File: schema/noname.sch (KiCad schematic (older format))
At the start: 7 parts

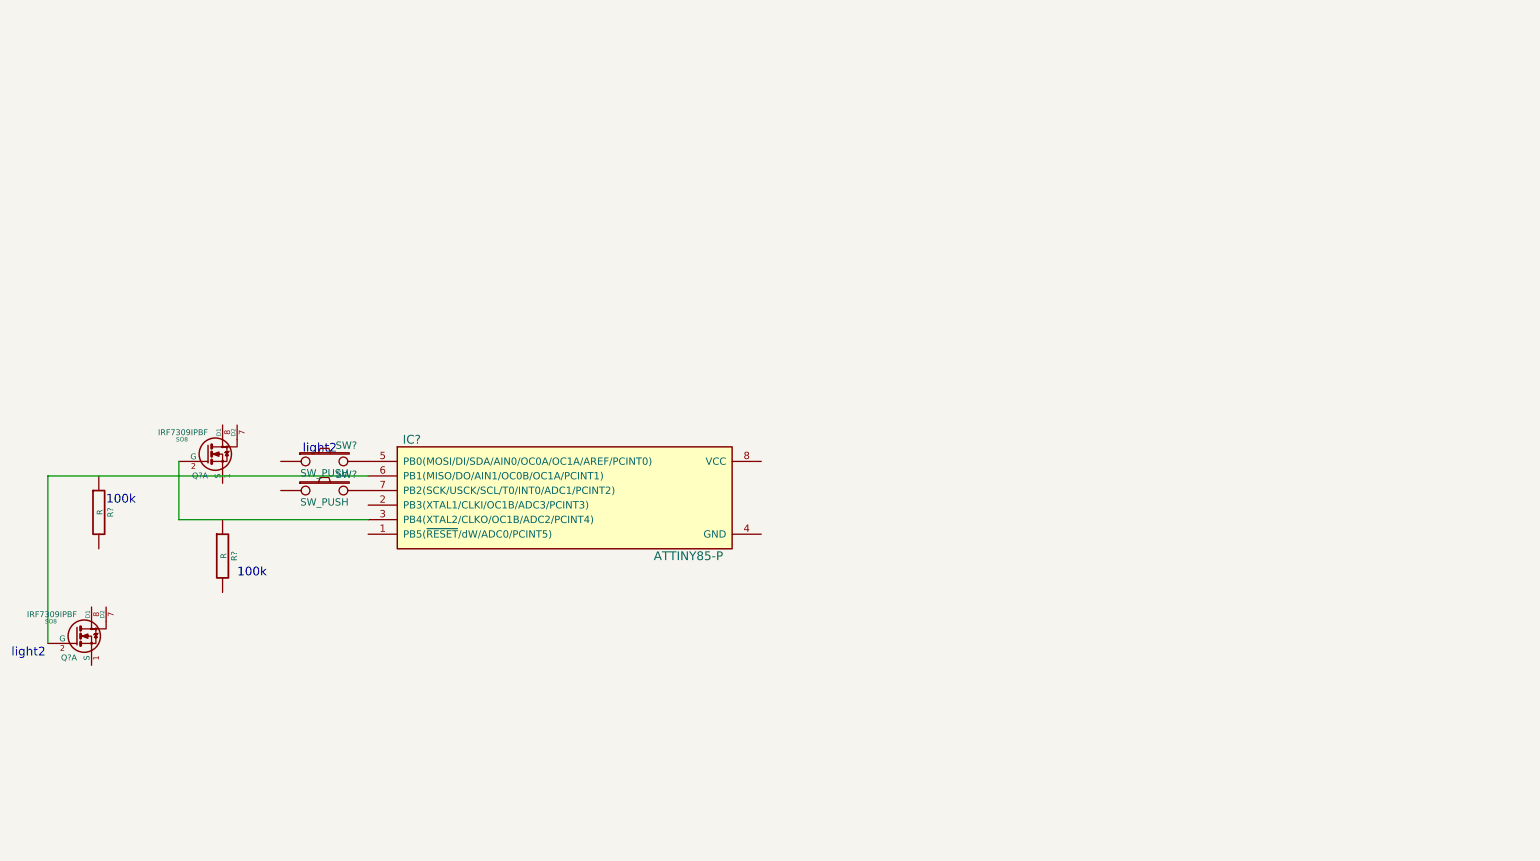
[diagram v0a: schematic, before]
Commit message: Use other pins
The Trinket boot makes the led flicker at startup (even without usb
connection). Use other pins that are not used by the boot software.
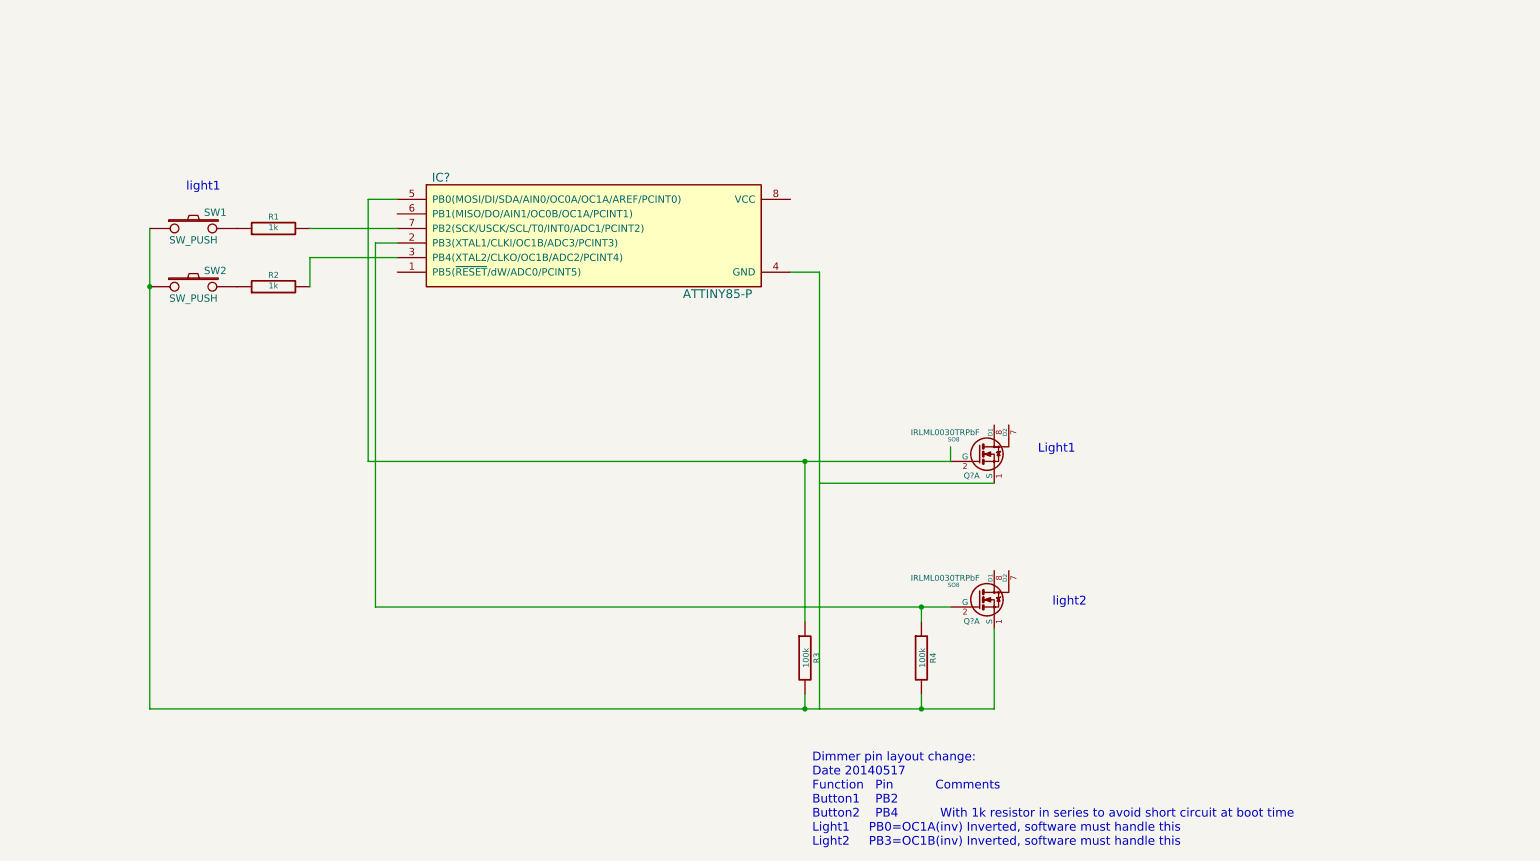
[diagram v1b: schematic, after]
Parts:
- added R1, R2: 1k, ~, symbol R
- Q? (x2): value IRF7309IPBF -> IRLML0030TRPbF
- R3, R4: renamed from R?; value R -> 100k
- gave numbers to parts that had none: 2
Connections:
- wire segments 4 -> 20
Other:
- note added: "Dimmer pin layout change:\nDate 20140517\nFunction Pin Comments\nButton1 PB2\nButton2 PB4 With 1k resistor in series to avoid short circuit at boot time\nLight1 PB0=OC1A(inv) Inverted, software must handle this\nLight2 PB3=OC1B(inv) Inverted, software must handle this"
- note added: "Light1"
- note added: "light1\n"
- note removed: "100k"
- note removed: "light2"
- moved on the sheet: IC?, Q?A, R3, R4, SW1, SW2
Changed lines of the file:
@@
 LIBS:contrib
 LIBS:valves
+LIBS:noname-cache
 EELAYER 27 0
 EELAYER END
@@
 Sheet 1 1
 Title "noname.sch"
-Date "15 may 2014"
+Date "17 may 2014"
 Rev ""
 Comp ""
@@
 L ATTINY85-P IC?
 U 1 1 53752E2B
-P 5050 3550
-F 0 "IC?" H 4000 3950 60  0000 C CNN
-F 1 "ATTINY85-P" H 5900 3150 60  0000 C CNN
-F 2 "DIP8" H 4000 3150 60  0001 C CNN
-F 3 "" H 5050 3550 60  0000 C CNN
-	1    5050 3550
+P 5250 1750
+F 0 "IC?" H 4200 2150 60  0000 C CNN
+F 1 "ATTINY85-P" H 6100 1350 60  0000 C CNN
+F 2 "DIP8" H 4200 1350 60  0001 C CNN
+F 3 "" H 5250 1750 60  0000 C CNN
+	1    5250 1750
 	1    0    0    -1
 $EndComp
@@
 L IRF7309IPBF Q?
 U 1 1 53752E93
-P 2600 3250
-F 0 "Q?" H 2600 3102 40  0000 R CNN
-F 1 "IRF7309IPBF" H 2600 3399 40  0000 R CNN
-F 2 "SO8" H 2421 3351 29  0000 C CNN
-F 3 "~" H 2600 3250 60  0000 C CNN
-	1    2600 3250
+P 7900 3250
+F 0 "Q?" H 7900 3102 40  0000 R CNN
+F 1 "IRLML0030TRPbF" H 7900 3399 40  0000 R CNN
+F 2 "SO8" H 7721 3351 29  0000 C CNN
+F 3 "~" H 7900 3250 60  0000 C CNN
+	1    7900 3250
 	1    0    0    -1
 $EndComp
-Wire Wire Line
-	3700 3700 2400 3700
-Wire Wire Line
-	2400 3700 2400 3300
 $Comp
 L IRF7309IPBF Q?
 U 1 1 53752F5C
-P 1700 4500
-F 0 "Q?" H 1700 4352 40  0000 R CNN
-F 1 "IRF7309IPBF" H 1700 4649 40  0000 R CNN
-F 2 "SO8" H 1521 4601 29  0000 C CNN
-F 3 "~" H 1700 4500 60  0000 C CNN
-	1    1700 4500
+P 7900 4250
+F 0 "Q?" H 7900 4102 40  0000 R CNN
+F 1 "IRLML0030TRPbF" H 7900 4399 40  0000 R CNN
+F 2 "SO8" H 7721 4351 29  0000 C CNN
+F 3 "~" H 7900 4250 60  0000 C CNN
+	1    7900 4250
 	1    0    0    -1
 $EndComp
 $Comp
-L R R?
+L R R4
 U 1 1 53753193
-P 2700 3950
-F 0 "R?" V 2780 3950 40  0000 C CNN
-F 1 "R" V 2707 3951 40  0000 C CNN
-F 2 "~" V 2630 3950 30  0000 C CNN
-F 3 "~" H 2700 3950 30  0000 C CNN
-	1    2700 3950
+P 7500 4650
+F 0 "R4" V 7580 4650 40  0000 C CNN
+F 1 "100k" V 7507 4651 40  0000 C CNN
+F 2 "~" V 7430 4650 30  0000 C CNN
+F 3 "~" H 7500 4650 30  0000 C CNN
+	1    7500 4650
 	1    0    0    -1
 $EndComp
 $Comp
-L SW_PUSH SW?
+L SW_PUSH SW1
 U 1 1 5375321D
-P 3400 3500
-F 0 "SW?" H 3550 3610 50  0000 C CNN
-F 1 "SW_PUSH" H 3400 3420 50  0000 C CNN
-F 2 "~" H 3400 3500 60  0000 C CNN
-F 3 "~" H 3400 3500 60  0000 C CNN
-	1    3400 3500
+P 2500 1700
+F 0 "SW1" H 2650 1810 50  0000 C CNN
+F 1 "SW_PUSH" H 2500 1620 50  0000 C CNN
+F 2 "~" H 2500 1700 60  0000 C CNN
+F 3 "~" H 2500 1700 60  0000 C CNN
+	1    2500 1700
 	1    0    0    -1
 $EndComp
 $Comp
-L SW_PUSH SW?
+L SW_PUSH SW2
 U 1 1 53753232
-P 3400 3300
-F 0 "SW?" H 3550 3410 50  0000 C CNN
-F 1 "SW_PUSH" H 3400 3220 50  0000 C CNN
-F 2 "~" H 3400 3300 60  0000 C CNN
-F 3 "~" H 3400 3300 60  0000 C CNN
-	1    3400 3300
+P 2500 2100
+F 0 "SW2" H 2650 2210 50  0000 C CNN
+F 1 "SW_PUSH" H 2500 2020 50  0000 C CNN
+F 2 "~" H 2500 2100 60  0000 C CNN
+F 3 "~" H 2500 2100 60  0000 C CNN
+	1    2500 2100
 	1    0    0    -1
 $EndComp
-Text Notes 3250 3250 0    60   ~ 0
-light2\n
-Text Notes 1250 4650 0    60   ~ 0
-light2
-Wire Wire Line
-	3700 3400 1500 3400
-Wire Wire Line
-	1500 3400 1500 4550
-Text Notes 2800 4100 0    60   ~ 0
-100k
 $Comp
-L R R?
+L R R3
 U 1 1 53753325
-P 1850 3650
-F 0 "R?" V 1930 3650 40  0000 C CNN
-F 1 "R" V 1857 3651 40  0000 C CNN
-F 2 "~" V 1780 3650 30  0000 C CNN
-F 3 "~" H 1850 3650 30  0000 C CNN
-	1    1850 3650
+P 6700 4650
+F 0 "R3" V 6780 4650 40  0000 C CNN
+F 1 "100k" V 6707 4651 40  0000 C CNN
+F 2 "~" V 6630 4650 30  0000 C CNN
+F 3 "~" H 6700 4650 30  0000 C CNN
+	1    6700 4650
 	1    0    0    -1
 $EndComp
-Text Notes 1900 3600 0    60   ~ 0
-100k
+Text Notes 6750 5950 0    60   ~ 0
+Dimmer pin layout change:\nDate 20140517\nFunction   Pin           Comments\nButton1    PB2\nButton2    PB4           With 1k resistor in series to avoid short circuit at boot time\nLight1     PB0=OC1A(inv) Inverted, software must handle this\nLight2     PB3=OC1B(inv) Inverted, software must handle this
+Text Notes 8400 4300 0    60   ~ 0
+light2\n
+Text Notes 2450 1450 0    60   ~ 0
+light1\n
+$Comp
+L R R1
+U 1 1 53772E95
+P 3050 1700
+F 0 "R1" V 3130 1700 40  0000 C CNN
+F 1 "1k" V 3057 1701 40  0000 C CNN
+F 2 "~" V 2980 1700 30  0000 C CNN
+F 3 "~" H 3050 1700 30  0000 C CNN
+	1    3050 1700
+	0    -1   -1   0
+$EndComp
+$Comp
+L R R2
+U 1 1 53772EA2
+P 3050 2100
+F 0 "R2" V 3130 2100 40  0000 C CNN
+F 1 "1k" V 3057 2101 40  0000 C CNN
+F 2 "~" V 2980 2100 30  0000 C CNN
+F 3 "~" H 3050 2100 30  0000 C CNN
+	1    3050 2100
+	0    -1   -1   0
+$EndComp
+Wire Wire Line
+	3300 1700 3900 1700
+Wire Wire Line
+	3300 2100 3300 1900
+Wire Wire Line
+	3300 1900 3900 1900
+Wire Wire Line
+	7700 3200 7700 3300
+Wire Wire Line
+	3900 1500 3700 1500
+Wire Wire Line
+	3700 1500 3700 3300
+Wire Wire Line
+	3700 3300 7700 3300
+Wire Wire Line
+	3900 1800 3750 1800
+Wire Wire Line
+	3750 1800 3750 4300
+Wire Wire Line
+	3750 4300 7700 4300
+Wire Wire Line
+	6700 4400 6700 3300
+Connection ~ 6700 3300
+Wire Wire Line
+	7500 4400 7500 4300
+Connection ~ 7500 4300
+Wire Wire Line
+	8000 3450 6800 3450
+Wire Wire Line
+	6800 2000 6800 5000
+Wire Wire Line
+	6800 2000 6600 2000
+Wire Wire Line
+	6700 4900 6700 5000
+Wire Wire Line
+	2200 5000 8000 5000
+Wire Wire Line
+	7500 5000 7500 4900
+Wire Wire Line
+	8000 5000 8000 4450
+Connection ~ 7500 5000
+Wire Wire Line
+	2200 1700 2200 5000
+Connection ~ 6700 5000
+Connection ~ 2200 2100
+Text Notes 8300 3250 0    60   ~ 0
+Light1
 $EndSCHEMATC

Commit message: added fet footprint in schema
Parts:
- removed Q? (x2): IRLML0030TRPbF, SO8, symbol IRF7309IPBF
- added Q? (x2): IRLML0030TRPBF, SOT-23, symbol IRLML0030TRPBF
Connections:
- wire segments 20 -> 21
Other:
- note added: "1"
- note added: "2"
- note added: "3"
- note added: "SOT-23"
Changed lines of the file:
@@
-$EndComp
-$Comp
-L IRF7309IPBF Q?
-U 1 1 53752E93
-P 7900 3250
-F 0 "Q?" H 7900 3102 40  0000 R CNN
-F 1 "IRLML0030TRPbF" H 7900 3399 40  0000 R CNN
-F 2 "SO8" H 7721 3351 29  0000 C CNN
-F 3 "~" H 7900 3250 60  0000 C CNN
-	1    7900 3250
-	1    0    0    -1
-$EndComp
-$Comp
-L IRF7309IPBF Q?
-U 1 1 53752F5C
-P 7900 4250
-F 0 "Q?" H 7900 4102 40  0000 R CNN
-F 1 "IRLML0030TRPbF" H 7900 4399 40  0000 R CNN
-F 2 "SO8" H 7721 4351 29  0000 C CNN
-F 3 "~" H 7900 4250 60  0000 C CNN
-	1    7900 4250
-	1    0    0    -1
 $EndComp
 $Comp
@@
 Text Notes 8300 3250 0    60   ~ 0
 Light1
+$Comp
+L IRLML0030TRPBF Q?
+U 1 1 53774EA5
+P 7900 3150
+F 0 "Q?" H 7900 3002 40  0000 R CNN
+F 1 "IRLML0030TRPBF" H 7900 3299 40  0000 R CNN
+F 2 "SOT-23" H 7721 3251 29  0000 C CNN
+F 3 "~" H 7900 3150 60  0000 C CNN
+	1    7900 3150
+	1    0    0    -1
+$EndComp
+$Comp
+L IRLML0030TRPBF Q?
+U 1 1 53774EB4
+P 7900 4250
+F 0 "Q?" H 7900 4102 40  0000 R CNN
+F 1 "IRLML0030TRPBF" H 7900 4399 40  0000 R CNN
+F 2 "SOT-23" H 7721 4351 29  0000 C CNN
+F 3 "~" H 7900 4250 60  0000 C CNN
+	1    7900 4250
+	1    0    0    -1
+$EndComp
+Wire Wire Line
+	8000 3450 8000 3350
+Wire Notes Line
+	7100 2200 7400 2200
+Wire Notes Line
+	7400 2200 7400 2650
+Wire Notes Line
+	7400 2650 7100 2650
+Wire Notes Line
+	7100 2650 7100 2200
+Wire Notes Line
+	7100 2300 7050 2300
+Wire Notes Line
+	7050 2300 7050 2350
+Wire Notes Line
+	7050 2350 7100 2350
+Wire Notes Line
+	7100 2550 7050 2550
+Wire Notes Line
+	7050 2550 7050 2500
+Wire Notes Line
+	7050 2500 7100 2500
+Wire Notes Line
+	7400 2400 7450 2400
+Wire Notes Line
+	7450 2400 7450 2450
+Wire Notes Line
+	7450 2450 7400 2450
+Text Notes 6950 2300 0    60   ~ 0
+1
+Text Notes 6950 2550 0    60   ~ 0
+2
+Text Notes 7500 2400 0    60   ~ 0
+3
+Text Notes 7000 2100 0    60   ~ 0
+SOT-23
+Connection ~ 6800 5000
+Connection ~ 6700 4400
+Connection ~ 7500 4400
+Connection ~ 7500 4900
+Connection ~ 6700 4900
+Connection ~ 7700 4300
+Connection ~ 8000 4450
+Connection ~ 6800 3450
+Connection ~ 7700 3200
+Connection ~ 8000 3350
+Connection ~ 6600 2000
+Connection ~ 3900 1900
+Connection ~ 3900 1800
+Connection ~ 3900 1700
+Connection ~ 3900 1500
+Connection ~ 3300 1700
+Connection ~ 3300 2100
+Connection ~ 2800 2100
+Connection ~ 2800 1700
+Connection ~ 2200 1700
 $EndSCHEMATC

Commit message: Schema updated, software updated
This works (tested) for light 1.
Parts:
- added R5, R6: 22k, ~, symbol R
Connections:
- wire segments 21 -> 20
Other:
- moved on the sheet: R4
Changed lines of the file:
@@
 Sheet 1 1
 Title "noname.sch"
-Date "17 may 2014"
+Date "22 may 2014"
 Rev ""
 Comp ""
@@
 L R R4
 U 1 1 53753193
-P 7500 4650
-F 0 "R4" V 7580 4650 40  0000 C CNN
-F 1 "100k" V 7507 4651 40  0000 C CNN
-F 2 "~" V 7430 4650 30  0000 C CNN
-F 3 "~" H 7500 4650 30  0000 C CNN
-	1    7500 4650
+P 7000 4650
+F 0 "R4" V 7080 4650 40  0000 C CNN
+F 1 "100k" V 7007 4651 40  0000 C CNN
+F 2 "~" V 6930 4650 30  0000 C CNN
+F 3 "~" H 7000 4650 30  0000 C CNN
+	1    7000 4650
 	1    0    0    -1
 $EndComp
@@
 	3300 1900 3900 1900
 Wire Wire Line
-	7700 3200 7700 3300
-Wire Wire Line
 	3900 1500 3700 1500
 Wire Wire Line
-	3700 1500 3700 3300
-Wire Wire Line
-	3700 3300 7700 3300
-Wire Wire Line
 	3900 1800 3750 1800
 Wire Wire Line
 	3750 1800 3750 4300
 Wire Wire Line
-	3750 4300 7700 4300
-Wire Wire Line
-	6700 4400 6700 3300
-Connection ~ 6700 3300
-Wire Wire Line
-	7500 4400 7500 4300
-Connection ~ 7500 4300
-Wire Wire Line
 	8000 3450 6800 3450
 Wire Wire Line
@@
 	2200 5000 8000 5000
 Wire Wire Line
-	7500 5000 7500 4900
-Wire Wire Line
 	8000 5000 8000 4450
-Connection ~ 7500 5000
 Wire Wire Line
 	2200 1700 2200 5000
@@
 Connection ~ 6800 5000
 Connection ~ 6700 4400
-Connection ~ 7500 4400
-Connection ~ 7500 4900
 Connection ~ 6700 4900
 Connection ~ 7700 4300
@@
 Connection ~ 2800 1700
 Connection ~ 2200 1700
+$Comp
+L R R5
+U 1 1 537E6BFB
+P 7450 3200
+F 0 "R5" V 7530 3200 40  0000 C CNN
+F 1 "22k" V 7457 3201 40  0000 C CNN
+F 2 "~" V 7380 3200 30  0000 C CNN
+F 3 "~" H 7450 3200 30  0000 C CNN
+	1    7450 3200
+	0    -1   -1   0
+$EndComp
+$Comp
+L R R6
+U 1 1 537E6C0A
+P 7450 4300
+F 0 "R6" V 7530 4300 40  0000 C CNN
+F 1 "22k" V 7457 4301 40  0000 C CNN
+F 2 "~" V 7380 4300 30  0000 C CNN
+F 3 "~" H 7450 4300 30  0000 C CNN
+	1    7450 4300
+	0    -1   -1   0
+$EndComp
+Wire Wire Line
+	7200 3200 3700 3200
+Connection ~ 3700 3200
+Wire Wire Line
+	3700 3200 3700 1500
+Wire Wire Line
+	6700 4400 6700 3200
+Connection ~ 6700 3200
+Wire Wire Line
+	7000 4900 7000 5000
+Connection ~ 7000 5000
+Wire Wire Line
+	7000 4400 7000 4300
+Connection ~ 7000 4300
+Wire Wire Line
+	3750 4300 7200 4300
+Connection ~ 7200 4300
+Connection ~ 7000 4400
+Connection ~ 7000 4900
+Connection ~ 7200 3200
 $EndSCHEMATC

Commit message: Fade out implemented
But I don't like it, it flickers too much (due to pwm in attiny?)
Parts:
- added C?: C, ~, symbol C
- added D?: ZENERSMALL, ~, symbol ZENERSMALL
- added D? (x2): 3.0V, ~, symbol ZENER
- added D?: RED, ~, symbol LED
- added D?: GREEN, ~, symbol LED
- added J?: USB, symbol USB
- added R1, R2: 68, ~, symbol R
- added R1, R11: 470, ~, symbol R
- added R3: 1k5, ~, symbol R
- renumbered R1 to R11, R2 to R12, R3 to R13, R4 to R14, R5 to R15, R6 to R16
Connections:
- wire segments 20 -> 35
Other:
- note added: "+5V"
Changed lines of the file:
@@
 Sheet 1 1
 Title "noname.sch"
-Date "22 may 2014"
+Date "25 may 2014"
 Rev ""
 Comp ""
@@
 $EndComp
 $Comp
-L R R4
+L R R14
 U 1 1 53753193
 P 7000 4650
-F 0 "R4" V 7080 4650 40  0000 C CNN
+F 0 "R14" V 7080 4650 40  0000 C CNN
 F 1 "100k" V 7007 4651 40  0000 C CNN
 F 2 "~" V 6930 4650 30  0000 C CNN
@@
 $EndComp
 $Comp
-L R R3
+L R R13
 U 1 1 53753325
 P 6700 4650
-F 0 "R3" V 6780 4650 40  0000 C CNN
+F 0 "R13" V 6780 4650 40  0000 C CNN
 F 1 "100k" V 6707 4651 40  0000 C CNN
 F 2 "~" V 6630 4650 30  0000 C CNN
@@
 light1\n
 $Comp
-L R R1
+L R R11
 U 1 1 53772E95
 P 3050 1700
-F 0 "R1" V 3130 1700 40  0000 C CNN
+F 0 "R11" V 3130 1700 40  0000 C CNN
 F 1 "1k" V 3057 1701 40  0000 C CNN
 F 2 "~" V 2980 1700 30  0000 C CNN
@@
 $EndComp
 $Comp
-L R R2
+L R R12
 U 1 1 53772EA2
 P 3050 2100
-F 0 "R2" V 3130 2100 40  0000 C CNN
+F 0 "R12" V 3130 2100 40  0000 C CNN
 F 1 "1k" V 3057 2101 40  0000 C CNN
 F 2 "~" V 2980 2100 30  0000 C CNN
@@
 Wire Wire Line
 	3900 1800 3750 1800
-Wire Wire Line
-	3750 1800 3750 4300
 Wire Wire Line
 	8000 3450 6800 3450
@@
 Connection ~ 2200 1700
 $Comp
-L R R5
+L R R15
 U 1 1 537E6BFB
 P 7450 3200
-F 0 "R5" V 7530 3200 40  0000 C CNN
+F 0 "R15" V 7530 3200 40  0000 C CNN
 F 1 "22k" V 7457 3201 40  0000 C CNN
 F 2 "~" V 7380 3200 30  0000 C CNN
@@
 $EndComp
 $Comp
-L R R6
+L R R16
 U 1 1 537E6C0A
 P 7450 4300
-F 0 "R6" V 7530 4300 40  0000 C CNN
+F 0 "R16" V 7530 4300 40  0000 C CNN
 F 1 "22k" V 7457 4301 40  0000 C CNN
 F 2 "~" V 7380 4300 30  0000 C CNN
@@
 Connection ~ 7000 4900
 Connection ~ 7200 3200
+$Comp
+L R R11
+U 1 1 5381B948
+P 3550 4350
+F 0 "R11" V 3630 4350 40  0000 C CNN
+F 1 "470" V 3557 4351 40  0000 C CNN
+F 2 "~" V 3480 4350 30  0000 C CNN
+F 3 "~" H 3550 4350 30  0000 C CNN
+	1    3550 4350
+	1    0    0    -1
+$EndComp
+$Comp
+L R R2
+U 1 1 5381B957
+P 3300 2350
+F 0 "R2" V 3380 2350 40  0000 C CNN
+F 1 "68" V 3307 2351 40  0000 C CNN
+F 2 "~" V 3230 2350 30  0000 C CNN
+F 3 "~" H 3300 2350 30  0000 C CNN
+	1    3300 2350
+	1    0    0    -1
+$EndComp
+$Comp
+L R R1
+U 1 1 5381B967
+P 4200 2450
+F 0 "R1" V 4280 2450 40  0000 C CNN
+F 1 "68" V 4207 2451 40  0000 C CNN
+F 2 "~" V 4130 2450 30  0000 C CNN
+F 3 "~" H 4200 2450 30  0000 C CNN
+	1    4200 2450
+	1    0    0    -1
+$EndComp
+$Comp
+L R R3
+U 1 1 5381B976
+P 4350 4350
+F 0 "R3" V 4430 4350 40  0000 C CNN
+F 1 "1k5" V 4357 4351 40  0000 C CNN
+F 2 "~" V 4280 4350 30  0000 C CNN
+F 3 "~" H 4350 4350 30  0000 C CNN
+	1    4350 4350
+	1    0    0    -1
+$EndComp
+$Comp
+L R R1
+U 1 1 5381B985
+P 5500 2550
+F 0 "R1" V 5580 2550 40  0000 C CNN
+F 1 "470" V 5507 2551 40  0000 C CNN
+F 2 "~" V 5430 2550 30  0000 C CNN
+F 3 "~" H 5500 2550 30  0000 C CNN
+	1    5500 2550
+	1    0    0    -1
+$EndComp
+$Comp
+L ZENERSMALL D?
+U 1 1 5381B994
+P 5600 800
+F 0 "D?" H 5600 900 40  0000 C CNN
+F 1 "ZENERSMALL" H 5600 700 30  0000 C CNN
+F 2 "~" H 5600 800 60  0000 C CNN
+F 3 "~" H 5600 800 60  0000 C CNN
+	1    5600 800
+	1    0    0    -1
+$EndComp
+$Comp
+L ZENER D?
+U 1 1 5381B9A3
+P 4200 4800
+F 0 "D?" H 4200 4900 50  0000 C CNN
+F 1 "3.0V" H 4200 4700 40  0000 C CNN
+F 2 "~" H 4200 4800 60  0000 C CNN
+F 3 "~" H 4200 4800 60  0000 C CNN
+	1    4200 4800
+	0    -1   -1   0
+$EndComp
+$Comp
+L ZENER D?
+U 1 1 5381B9B2
+P 3300 4800
+F 0 "D?" H 3300 4900 50  0000 C CNN
+F 1 "3.0V" H 3300 4700 40  0000 C CNN
+F 2 "~" H 3300 4800 60  0000 C CNN
+F 3 "~" H 3300 4800 60  0000 C CNN
+	1    3300 4800
+	0    -1   -1   0
+$EndComp
+$Comp
+L LED D?
+U 1 1 5381B9C1
+P 3550 4800
+F 0 "D?" H 3550 4900 50  0000 C CNN
+F 1 "RED" H 3550 4700 50  0000 C CNN
+F 2 "~" H 3550 4800 60  0000 C CNN
+F 3 "~" H 3550 4800 60  0000 C CNN
+	1    3550 4800
+	0    1    1    0
+$EndComp
+$Comp
+L LED D?
+U 1 1 5381B9D0
+P 5500 4800
+F 0 "D?" H 5500 4900 50  0000 C CNN
+F 1 "GREEN" H 5500 4700 50  0000 C CNN
+F 2 "~" H 5500 4800 60  0000 C CNN
+F 3 "~" H 5500 4800 60  0000 C CNN
+	1    5500 4800
+	0    1    1    0
+$EndComp
+Wire Wire Line
+	3550 1600 3900 1600
+Connection ~ 3650 5000
+$Comp
+L USB J?
+U 1 1 5381BBAC
+P 2600 3650
+F 0 "J?" H 2550 4050 60  0000 C CNN
+F 1 "USB" V 2350 3800 60  0000 C CNN
+F 2 "" H 2600 3650 60  0000 C CNN
+F 3 "" H 2600 3650 60  0000 C CNN
+	1    2600 3650
+	0    -1   -1   0
+$EndComp
+Wire Wire Line
+	3300 2600 3300 4600
+Wire Wire Line
+	4200 2200 3750 2200
+Connection ~ 3750 2200
+Wire Wire Line
+	4200 2700 4200 4600
+Connection ~ 3750 1800
+$Comp
+L C C?
+U 1 1 5381BD85
+P 5800 2500
+F 0 "C?" H 5800 2600 40  0000 L CNN
+F 1 "C" H 5806 2415 40  0000 L CNN
+F 2 "~" H 5838 2350 30  0000 C CNN
+F 3 "~" H 5800 2500 60  0000 C CNN
+	1    5800 2500
+	1    0    0    -1
+$EndComp
+Wire Wire Line
+	6600 1500 6700 1500
+Wire Wire Line
+	6700 1500 6700 2300
+Wire Wire Line
+	6700 2300 5500 2300
+Wire Wire Line
+	5500 2800 5500 4600
+Wire Wire Line
+	5800 2700 5800 5000
+Connection ~ 5800 5000
+Wire Wire Line
+	2800 3300 2800 3000
+Wire Wire Line
+	2800 3000 3300 3000
+Connection ~ 3300 3000
+Wire Wire Line
+	2950 3300 2950 3100
+Wire Wire Line
+	2950 3100 4200 3100
+Connection ~ 4200 3100
+Wire Wire Line
+	3750 1800 3750 4300
+Wire Wire Line
+	4200 4600 4350 4600
+Text Notes 4350 4050 0    60   ~ 0
++5V
+Wire Wire Line
+	3550 4100 3550 1600
 $EndSCHEMATC
